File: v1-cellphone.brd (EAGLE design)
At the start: 91.4 x 44.5 mm, 55 parts, among them J1 AVRISP, J2 ZX62D-B-5P8, U1 MCP73831, U2 MEGA1284, U3 GSM_UC15, X1 BU-SMA-V, X2 CRYSTAL, X3 CCM03-3002 R102

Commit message: Ready for review at diy devices.
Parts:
- added C10: 18pF, rcl_custom:C0603
- added C17, C18: 100nF, cellphone-rcl:C1206
- added C19, C23: 100nF 16V, cellphone-rcl:C1206
- added C20, C24: 33pF 16V, cellphone-rcl:C1206
- added C21, C25: 10pF 16V, cellphone-rcl:C1206
- added C22, C26: 100uF 16V, cellphone-rcl:C1206
- added D1, D2, D3: (no value), SparkFun-DiscreteSemi:SMA-DIODE
- added D4: 5.1V, SparkFun-DiscreteSemi:SMB-DIODE
- added R11: 100, v1-cellphone:CELLPHONE-RCL_R1206
- added R12: 2K, v1-cellphone:CELLPHONE-RCL_R1206
- added TP1, TP2, TP3: TPPAD1-13, testpad:P1-13
- C12, C5: value 0.1uF -> 100nF
- C14: device cellphone-rcl:C1206 -> rcl_custom:C0603
- C15: value 18pF -> 100nF
- S1: device cellphone:B3U-1000P -> v1-cellphone:CELLPHONE_B3U-1000P
- X2: value CRYSTAL -> 16MHz
- moved C15 176.3 mm to (-54.6, -114.6), turned to 0 degrees
- moved C14 165.2 mm to (-55.6, -109.0), turned to 0 degrees
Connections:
- removed net SPK2P: U3.20
- removed net VCC: C11.+, C12.1, C13.1, C16.+, C4.1, J1.2, JP3.1, JP8.1, JP9.1, LED3.A, R4.2, U1.3, U2.17, U2.27, U2.38, U2.5
- removed net VDD_EXT: U3.7
- removed net VUSB: C3.1, J2.P1, LED1.A, U1.4
- new net 4.2V: C4.1, R11.2, U1.3
- new net 4V: C11.+, C12.1, C13.1, C15.1, C16.+, C17.1, C18.1, C19.1, C20.1, C21.1, C22.1, C23.1, C24.1, C25.1, C26.1, D4.C, JP3.1, JP8.1, JP9.1, LED3.A, R11.1, R12.2, R4.2, U2.17, U2.27, U2.38, U2.5, U3.50, U3.51, U3.52, U3.53
- new net 5V: C3.1, D1.C, D2.C, D3.C, LED1.A, U1.4
- new net N$10: D2.A, J1.2
- new net N$11: D3.A, JP7.4
- new net N$13: TP1.TP, U3.2
- new net N$14: TP2.TP, U3.7
- new net N$15: TP3.TP, U3.55
- new net N$9: D1.A, J2.P1
- net AGND: no longer U2.29
- net GND: now also C10.2, C17.2, C18.2, C19.2, C20.2, C21.2, C22.2, C23.2, C24.2, C25.2, C26.2, C5.1, D4.A, R12.1, U2.29; no longer C5.2
- net N$7: now also C10.1, X2.P$1; no longer C15.1, X2.P$2
- net N$8: now also X2.P$2; no longer X2.P$1
- net SHLD: now also C5.2; no longer C5.1
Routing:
- net VCC: track 111.3 -> 0.00 mm, vias 6 -> 0
- net 4V: track 0.00 -> 48.7 mm, vias 0 -> 5
- net VUSB: track 23.8 -> 0.00 mm
- net 5V: track 0.00 -> 23.8 mm
- net GND: track 38.9 -> 17.2 mm, vias 36 -> 35
- net N$8: track 8.00 -> 0.00 mm
- net N$7: track 7.92 -> 0.00 mm
- added copper zone on layer 1, net 4V
- added copper zone on layer 16, net 4V
- removed copper zone on layer 1, net VCC
- removed copper zone on layer 16, net VCC

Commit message: Added notes.
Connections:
- net RESET renamed !RESET
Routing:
- net !RESET: track 21.0 -> 18.3 mm
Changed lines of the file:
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@@
 <wire x1="34.036" y1="36.433" x2="-52.832" y2="-61.722" width="0" layer="19" extent="1-1"/>
 </signal>
-<signal name="RESET">
-<contactref element="R4" pad="1"/>
+<signal name="!RESET">
 <contactref element="C1" pad="2"/>
 <wire x1="47.879" y1="35.671" x2="47.879" y2="33.655" width="0.254" layer="1"/>
 <wire x1="47.879" y1="33.655" x2="47.879" y2="29.591" width="0.254" layer="1"/>
 <wire x1="47.879" y1="29.591" x2="50.188" y2="29.591" width="0.254" layer="1"/>
-<wire x1="38.109" y1="28.194" x2="37.855" y2="30.715" width="0.254" layer="16"/>
-<wire x1="37.855" y1="30.715" x2="37.954" y2="30.715" width="0.254" layer="16"/>
 <wire x1="47.879" y1="35.671" x2="39.732" y2="35.671" width="0.254" layer="1"/>
 <wire x1="46.088" y1="33.636" x2="47.86" y2="33.636" width="0.254" layer="1"/>
@@
 <contactref element="S1" pad="P$2"/>
 <contactref element="U2" pad="4"/>
+<contactref element="R4" pad="1"/>
 <wire x1="38.022" y1="28.194" x2="-50.292" y2="-64.262" width="0" layer="19" extent="16-16"/>
-<wire x1="38.109" y1="28.194" x2="38.022" y2="28.194" width="0" layer="19" extent="16-16"/>
-<wire x1="39.732" y1="35.671" x2="37.954" y2="30.715" width="0" layer="19" extent="1-16"/>
+<wire x1="37.855" y1="30.715" x2="38.022" y2="28.194" width="0" layer="19" extent="16-16"/>
+<wire x1="39.732" y1="35.671" x2="37.855" y2="30.715" width="0" layer="19" extent="1-16"/>
 <wire x1="50.188" y1="29.556" x2="50.188" y2="29.591" width="0" layer="19" extent="1-1"/>
 </signal>

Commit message: Version 1.2 with diode and power changes, package fixes to 0603.
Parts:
- removed D1, D2, D3: (no value), SparkFun-DiscreteSemi:SMA-DIODE
- removed D4: 5.1V, SparkFun-DiscreteSemi:SMB-DIODE
- removed JP1, JP5: (no value), pinhead:1X04
- removed JP2: (no value), v1-cellphone:PINHEAD_1X08
- removed JP4: (no value), pinhead:1X03
- removed JP6: (no value), v1-cellphone:PINHEAD_1X04
- removed JP8, JP9: BATTERY INPUT, SparkFun-Connectors:JST-2-SMD
- removed L23: 6.8nH Murata LQG18HN6N8J00D, SmartPrj:R0603-ROUND
- removed L24: 3.3nH Murata LQG18HN3N3S00D, SmartPrj:R0603-ROUND
- removed MIC1, MIC2, SPK: (no value), pinhead:1X02
- added C27, C28, C29, C33, C34, C35: 33pF 10V, rcl_custom:0603-B
- added C30, C31, C32, C36, C37, C38: 10pF 10V, rcl_custom:0603-B
- added J3: PA, SparkFun-Connectors:1X08_LOCK_LONGPADS
- added J4: PB, SparkFun-Connectors:1X04_LOCK_LONGPADS
- added J5: PC1, SparkFun-Connectors:1X03_LOCK_LONGPADS
- added J6: PC2, SparkFun-Connectors:1X04_LOCK_LONGPADS
- added J7: PD, SparkFun-Connectors:1X04_LOCK_LONGPADS
- added L1: 6.8nH Murata LQG18HN6N8J00D, rcl_custom:0603-B
- added L2: 3.3nH Murata LQG18HN3N3S00D, rcl_custom:0603-B
- added LED6: VCC, adafruit:CHIP-LED0603
- added Q1: MIC, adafruit:9.7ELECTRET
- added R13: 470, rcl_custom:0603-B
- added R14: 0 ohm, rcl_custom:0603-B
- added TP4, TP5, TP6, TP7, TP8, TP9: TPPAD1-13, testpad:P1-13
- C1: value 0.1 uF -> 100nF 16V; device cellphone-rcl:C1206 -> rcl_custom:0603-B
- C10, C14: device rcl_custom:C0603 -> rcl_custom:0603-B
- C12, C15, C17, C18, C5: value 100nF -> 100nF 16V; device cellphone-rcl:C1206 -> rcl_custom:0603-B
- C13: value 100nF 50V -> 100nF 16V; device cellphone-rcl:C1206 -> rcl_custom:0603-B
- C19, C20, C21, C22, C23, C24, C25, C26, C3, C4: device cellphone-rcl:C1206 -> rcl_custom:0603-B
- C2: value 100nF 50V -> 100nF 10V; device cellphone-rcl:C1206 -> rcl_custom:0603-B
- C6, C7, C9: value 33pF -> 33pF 10V; device cellphone-rcl:C1206 -> rcl_custom:0603-B
- C8: device SmartPrj:C0603-ROUND -> rcl_custom:0603-B
- J8: value (none) -> FTDI
- LED1: value (none) -> 5V; device v1-cellphone:CELLPHONE-LED_CHIP-LED0603 -> adafruit:CHIP-LED0603
- LED2: value (none) -> 3GSTAT; device cellphone-led:1206 -> adafruit:CHIP-LED0603
- LED3: value PWR -> VBAT; device cellphone-led:1206 -> adafruit:CHIP-LED0603
- LED4: value 13 -> DEBUG; device cellphone-led:1206 -> adafruit:CHIP-LED0603
- LED5: value (none) -> NETLIGHT; device cellphone-led:1206 -> adafruit:CHIP-LED0603
- R1, R10, R2, R3, R4, R5, R6, R9: device cellphone-rcl:R1206 -> rcl_custom:0603-B
- R11, R7, R8: device v1-cellphone:CELLPHONE-RCL_R1206 -> rcl_custom:0603-B
- R12: value 2K -> 2000; device v1-cellphone:CELLPHONE-RCL_R1206 -> rcl_custom:0603-B
- moved C1 256.3 mm to (-54.6, -202.7)
- moved R11 221.5 mm to (-54.6, -303.8)
- moved R12 221.5 mm to (-54.6, -309.9)
- renumbered JP3 to J9, JP7 to J8, SPEAKER to SP1
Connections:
- removed net 4.2V: C4.1, R11.2, U1.3
- removed net 4V: C11.+, C12.1, C13.1, C15.1, C16.+, C17.1, C18.1, C19.1, C20.1, C21.1, C22.1, C23.1, C24.1, C25.1, C26.1, D4.C, J9.1, JP8.1, JP9.1, LED3.A, R11.1, R12.2, R4.2, U2.17, U2.27, U2.38, U2.5, U3.50, U3.51, U3.52, U3.53
- removed net ANTENA: ANT1.FEED, C8.2, L24.2, X1.1
- removed net MIC1N: MIC2.2, U3.24
- removed net MIC1P: MIC2.1, U3.23
- removed net MIC2N: MIC1.2, U3.26
- removed net MIC2P: MIC1.1, U3.25
- removed net N$10: D2.A, J1.2
- removed net N$11: D3.A, J8.4
- new net ANTENNA: ANT1.FEED, C8.2, L2.2, X1.1
- new net N$16: C27.2, C28.1, C30.2, C31.1, Q1.+, U3.23
- new net N$19: C28.2, C29.1, C31.2, C32.1, Q1.-, U3.24
- new net STAT: R7.1, U1.1
- new net VBAT: C11.+, C13.1, C16.+, C4.1, J9.1, LED3.A, R11.2, U1.3
- new net VCC: C12.1, C15.1, C17.1, C18.1, C19.1, C20.1, C21.1, C22.1, C23.1, C24.1, C25.1, C26.1, LED6.A, R11.1, R12.2, R4.2, U2.17, U2.27, U2.38, U2.5, U3.50, U3.51, U3.52, U3.53
- net 5V: now also J1.2, J2.P1; no longer D1.C, D2.C, D3.C
- net AGND: now also C27.1, C29.2, C30.1, C32.2, C33.1, C35.2, C36.1, C38.2, L1.1, L2.1, R14.1; no longer L23.1, L24.1
- net ANT: now also L1.2; no longer L23.2
- net GND: now also R13.1, R14.2; no longer D4.A, JP8.2, JP9.2, R7.1, U1.1
- net N$9: now also LED6.C, R13.2; no longer D1.A, J2.P1
- net PA0: now also J3.1; no longer JP2.1
- net PA1: now also J3.2; no longer JP2.2
- net PA2: now also J3.3; no longer JP2.3
- net PA3: now also J3.4; no longer JP2.4
- net PA4: now also J3.5; no longer JP2.5
- net PA5: now also J3.6; no longer JP2.6
- net PA6: now also J3.7; no longer JP2.7
- net PA7: now also J3.8; no longer JP2.8
- net PB0: now also J4.1; no longer JP6.1
- net PB1: now also J4.2; no longer JP6.2
- net PB2: now also J4.3; no longer JP6.3
- net PB3: now also J4.4; no longer JP6.4
- net PC0: now also J5.1; no longer JP4.1
- net PC1: now also J5.2; no longer JP4.2
- net PC2: now also J5.3; no longer JP4.3
- net PC4: now also J6.1; no longer JP1.1
- net PC5: now also J6.2; no longer JP1.2
- net PC6: now also J6.3; no longer JP1.3
- net PC7: now also J6.4; no longer JP1.4
- net PD4: now also J7.1; no longer JP5.1
- net PD5: now also J7.2; no longer JP5.2
- net PD6: now also J7.3; no longer JP5.3
- net PD7: now also J7.4; no longer JP5.4
- net RXD1: now also TP5.TP
- net SIM_CLKR: now also TP8.TP
- net SIM_DATA: now also TP9.TP
- net SIM_RSTR: now also TP7.TP
- net SIM_VDD: now also TP6.TP
- net SPK1N: now also C34.2, C35.1, C37.2, C38.1; no longer SPK.1
- net SPK1P: now also C33.2, C34.1, C36.2, C37.1; no longer SPK.2
- net TXD1: now also TP4.TP
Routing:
- net PD5: track 61.5 -> 10.0 mm
- net VCC: track 0.00 -> 49.0 mm, vias 0 -> 5
- net 4V: track 48.7 -> 0.00 mm, vias 5 -> 0
- net SPK1N: track 24.2 -> 0.00 mm
- net SPK1P: track 20.6 -> 0.00 mm
- net !RESET: track 18.3 -> 0.00 mm
- net PC7: track 32.4 -> 16.2 mm
- net ANTENNA: track 0.00 -> 12.3 mm
- net ANTENA: track 12.1 -> 0.00 mm
- net PD4: track 19.5 -> 8.04 mm
- net PD6: track 20.9 -> 12.0 mm
- net PD7: track 21.6 -> 13.4 mm
- net PC1: track 24.4 -> 19.9 mm
- net PC2: track 27.4 -> 23.6 mm
- net PC4: track 25.8 -> 22.7 mm
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- added copper zone on layer 1, net VCC
- added copper zone on layer 16, net VCC
- removed copper zone on layer 1, net 4V
- removed copper zone on layer 16, net 4V

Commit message: Major power changes. Fixed 2.6V signal lines. Ready for review.
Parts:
- removed J6: PC2, SparkFun-Connectors:1X04_LOCK_LONGPADS
- removed J7: PD, SparkFun-Connectors:1X04_LOCK_LONGPADS
- removed LED6: VCC, adafruit:CHIP-LED0603
- added C39: 2.2uF, rcl_custom:0603-B
- added Q2, Q3: NTR4501N-D, max-viz:SOT-23
- added TP10, TP11, TP12, TP13, TP14, TP15, TP17: TPPAD1-13, testpad:P1-13
- added U4: TXB0104PWR, SparkFun-DigitalIC:TSSOP14
- C8: value 3.9pF Murata GQM1885C2A3R9BB01D -> 3.9pF 100V 0603
- J5: value PC1 -> PC; device SparkFun-Connectors:1X03_LOCK_LONGPADS -> SparkFun-Connectors:1X08_LOCK_LONGPADS
- L1: value 6.8nH Murata LQG18HN6N8J00D -> 6.8nH 430mA 0603
- L2: value 3.3nH Murata LQG18HN3N3S00D -> 3.3nH 500mA 0603
- R11: value 100 -> 4.99K
- R12: value 2000 -> 4.99K
- R13: value 470 -> 10K
- moved R11 195.3 mm to (-55.6, -499.1)
- moved R12 194.3 mm to (-55.6, -504.2)
- moved TP4 153.2 mm to (-55.4, -468.6)
- moved TP5 153.2 mm to (-55.4, -472.9)
- moved R13 122.9 mm to (-55.6, -509.3)
- moved J5 71.9 mm to (-55.4, -445.8)
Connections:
- removed net N$9: LED6.C, R13.2
- removed net PD4: J7.1, U2.13
- removed net PD5: J7.2, U2.14
- removed net PD6: J7.3, U2.15
- removed net PD7: J7.4, U2.16
- removed net PWRKEY: U2.22, U3.18
- removed net STAT: R7.1, U1.1
- removed net STATUS: LED2.A, U3.54
- removed net VCC: C12.1, C15.1, C17.1, C18.1, C19.1, C20.1, C21.1, C22.1, C23.1, C24.1, C25.1, C26.1, LED6.A, R11.1, R12.2, R4.2, U2.17, U2.27, U2.38, U2.5, U3.50, U3.51, U3.52, U3.53
- new net !PWRKEY: Q2.3, U3.18
- new net !UC15RESET: Q3.3, U3.17
- new net 2.6V: C39.1, R13.1, TP2.TP, U3.7, U4.1
- new net BATTSTATUS: R7.1, U1.1, U2.15
- new net N$10: TP10.TP, U3.11
- new net N$11: TP13.TP, X3.C6
- new net N$20: TP4.TP, U3.60, U4.2
- new net N$21: TP5.TP, U3.61, U4.3
- new net N$23: TP17.TP, U3.54, U4.5
- new net PC3: J5.4, U2.22
- new net SETPWRKEY: Q2.1, R11.2, TP12.TP, U2.13
- new net SETUC15RESET: Q3.1, R12.2, TP11.TP, U2.14
- new net UC15STATUS: LED2.A, U2.16, U4.10
- net 5V: now also J8.4
- net GND: now also C39.2, Q2.2, Q3.2, R11.1, U4.7; no longer R13.1
- net N$14: now also R13.2, U4.8; no longer TP2.TP, U3.7
- net PC4: now also J5.5; no longer J6.1
- net PC5: now also J5.6; no longer J6.2
- net PC6: now also J5.7; no longer J6.3
- net PC7: now also J5.8; no longer J6.4
- net RXD1: now also TP15.TP, U4.13; no longer TP5.TP, U3.60
- net TXD1: now also TP14.TP, U4.12; no longer TP4.TP, U3.61
- net VBAT: now also C12.1, C15.1, C17.1, C18.1, C19.1, C20.1, C21.1, C22.1, C23.1, C24.1, C25.1, C26.1, R4.2, U2.17, U2.27, U2.38, U2.5, U3.50, U3.51, U3.52, U3.53, U4.14; no longer R11.2
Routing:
- net VCC: track 49.0 -> 0.00 mm, vias 5 -> 0
- net VBAT: track 0.00 -> 49.0 mm, vias 0 -> 2
- net UC15STATUS: track 0.00 -> 19.4 mm
- net PWRKEY: track 19.3 -> 0.00 mm, vias 1 -> 0
- net BATTSTATUS: track 0.00 -> 13.8 mm
- net PD7: track 13.4 -> 0.00 mm
- net PD6: track 12.0 -> 0.00 mm
- net AGND: track 10.2 -> 0.00 mm
- net SETUC15RESET: track 0.00 -> 10.0 mm
- net PD5: track 10.0 -> 0.00 mm
- net SETPWRKEY: track 0.00 -> 8.04 mm
- net PD4: track 8.04 -> 0.00 mm
- net STATUS: track 6.03 -> 0.00 mm
- net STAT: track 1.82 -> 0.00 mm
- added copper zone on layer 1, net 3.8V
- added copper zone on layer 16, net 3.8V
- removed copper zone on layer 1, net VCC
- removed copper zone on layer 16, net VCC

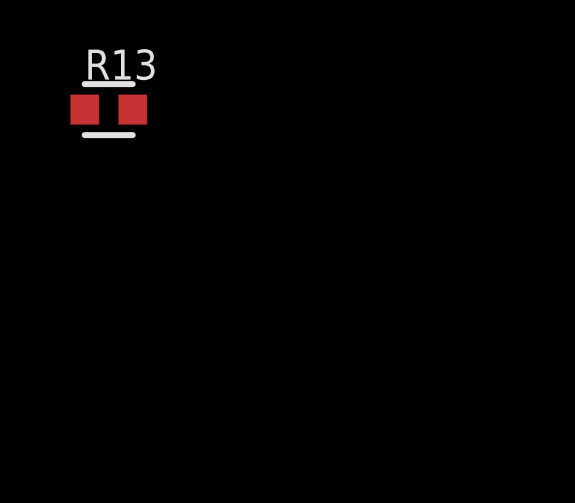
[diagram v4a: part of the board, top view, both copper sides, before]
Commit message: Added caps, made frames same size.
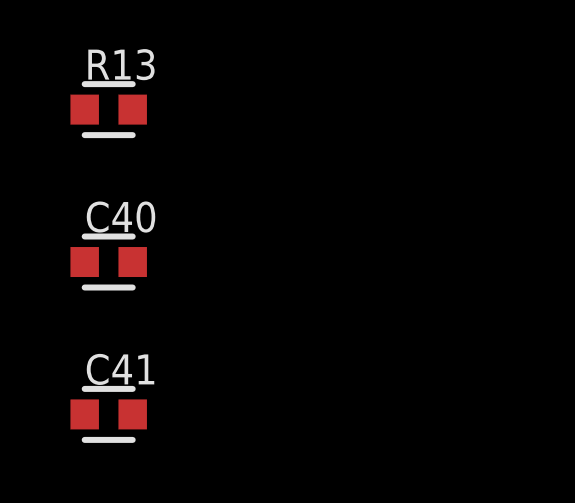
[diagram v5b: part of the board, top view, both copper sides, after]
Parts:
- added C40: 10nF 16V, rcl_custom:0603-B
- added C41: 100nF 16V, rcl_custom:0603-B
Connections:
- net !RESET: now also C40.1
- net GND: now also C40.2, C41.2
- net VBAT: now also C41.1
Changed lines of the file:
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@@
 <element name="R12" library="rcl_custom" package="0603-B" value="4.99K" x="-55.626" y="-504.19"/>
 <element name="R13" library="rcl_custom" package="0603-B" value="10K" x="-55.626" y="-509.27"/>
+<element name="C40" library="rcl_custom" package="0603-B" value="10nF 16V" x="-55.626" y="-514.35"/>
+<element name="C41" library="rcl_custom" package="0603-B" value="100nF 16V" x="-55.626" y="-519.43"/>
 </elements>
 <signals>
@@
 <via x="45.104" y="10.303" extent="1-16" drill="0.6096" shape="octagon"/>
 <via x="37.611" y="9.922" extent="1-16" drill="0.6096" shape="octagon"/>
-<contactref element="S1" pad="P$1"/>
 <contactref element="R10" pad="2"/>
 <polygon width="0.254" layer="16" isolate="0.254" thermals="no">
@@
 <contactref element="R12" pad="1"/>
 <contactref element="R11" pad="1"/>
+<contactref element="S1" pad="P$1"/>
+<contactref element="C40" pad="2"/>
+<contactref element="C41" pad="2"/>
 <wire x1="-53.81" y1="-169.418" x2="-53.81" y2="-175.514" width="0" layer="19" extent="1-1"/>
 <wire x1="-53.81" y1="-163.322" x2="-53.81" y2="-169.418" width="0" layer="19" extent="1-1"/>
@@
 <wire x1="-56.426" y1="-499.11" x2="-54.422" y2="-496.046" width="0" layer="19" extent="1-1"/>
 <wire x1="-56.426" y1="-504.19" x2="-56.426" y2="-499.11" width="0" layer="19" extent="1-1"/>
+<wire x1="-54.826" y1="-514.35" x2="-56.426" y2="-504.19" width="0" layer="19" extent="1-1"/>
+<wire x1="-54.826" y1="-519.43" x2="-54.826" y2="-514.35" width="0" layer="19" extent="1-1"/>
 </signal>
 <signal name="SIM_VDD">
@@
 <contactref element="J1" pad="5"/>
 <contactref element="C1" pad="2"/>
+<contactref element="R4" pad="1"/>
+<contactref element="C40" pad="1"/>
 <contactref element="S1" pad="P$2"/>
 <contactref element="U2" pad="4"/>
-<contactref element="R4" pad="1"/>
 <wire x1="38.022" y1="28.194" x2="-50.292" y2="-64.262" width="0" layer="19" extent="16-16"/>
 <wire x1="37.233" y1="30.715" x2="38.022" y2="28.194" width="0" layer="19" extent="16-16"/>
 <wire x1="50.188" y1="29.556" x2="38.022" y2="28.194" width="0" layer="19" extent="1-16"/>
 <wire x1="-53.81" y1="-202.692" x2="-50.292" y2="-64.262" width="0" layer="19" extent="1-1"/>
+<wire x1="-56.426" y1="-514.35" x2="-53.81" y2="-202.692" width="0" layer="19" extent="1-1"/>
 </signal>
 <signal name="N$5">
@@
 <wire x1="33.909" y1="35.306" x2="33.909" y2="37.468" width="0.254" layer="16"/>
 <contactref element="U4" pad="14"/>
+<contactref element="C41" pad="1"/>
 <wire x1="-55.41" y1="-169.418" x2="-55.41" y2="-175.514" width="0" layer="19" extent="1-1"/>
 <wire x1="-55.41" y1="-163.322" x2="-55.41" y2="-169.418" width="0" layer="19" extent="1-1"/>
@@
 <wire x1="87.11" y1="27.94" x2="61.788" y2="27.156" width="0" layer="19" extent="1-16"/>
 <wire x1="-54.782" y1="-483.7462" x2="-55.41" y2="-175.514" width="0" layer="19" extent="1-1"/>
+<wire x1="-56.426" y1="-519.43" x2="-54.782" y2="-483.7462" width="0" layer="19" extent="1-1"/>
 </signal>
 <signal name="BATTSTATUS" class="2">

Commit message: Verified packages. Minor tweaks throughout.
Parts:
- removed C16: 1mF 50V, cellphone-rcl:D/7343-31R
- removed J8: FTDI, cellphone:1X06-SMD-NOHOLES
- removed J9: BATTERY INPUT, SparkFun-Connectors:JST-2-SMD
- C11: device cellphone-rcl:D/7343-31R -> SparkFun-Capacitors:CPOL-RADIAL-1000UF-25V
- C2: value 100nF 10V -> 100nF 16V
- C27, C28, C29, C33, C35, C6, C7, C9: value 33pF 10V -> 33pF 16V
- C30: value 10pF 10V -> 10pF 10V
- C31, C32, C36, C37, C38: value 10pF 10V -> 10pF 16V
- C39: value 2.2uF -> 4.7uF 16V
- C4: value 4.7uF -> 4.7uF 16V
- J3: value PA -> GPIO; device SparkFun-Connectors:1X08_LOCK_LONGPADS -> SparkFun-Connectors:1X20_LOCK_LONGPADS
- J4: value PB -> FTDI; device SparkFun-Connectors:1X04_LOCK_LONGPADS -> SparkFun-Connectors:1X06_LOCK
- J5: value PC -> BATTERY INPUT; device SparkFun-Connectors:1X08_LOCK_LONGPADS -> SparkFun-Connectors:JST-2-SMD
- SP1: value SIREN -> SPEAKER
- X1: value BU-SMA-V -> SMA; device con-coax:BU-SMA-V -> v1-cellphone:CON-COAX_BU-SMA-V
- X2: value 16MHz -> 8MHz
- moved SP1 588.8 mm to (-54.4, -537.5), turned to 0 degrees
- moved Q2 513.0 mm to (78.2, 3.56)
- moved J5 488.3 mm to (5.33, 38.7), turned to 90 degrees
- moved C2 483.5 mm to (-55.6, -524.5)
- moved J4 398.8 mm to (89.2, 15.4), turned to 90 degrees
- moved J3 180.3 mm to (-55.4, -530.9)
- moved S1 55.8 mm to (88.4, 8.13)
- moved C11 16.3 mm to (19.4, 38.2)
- moved C3 1.83 mm to (15.7, 38.2)
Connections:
- net 5V: now also J4.4; no longer J8.4
- net GND: now also C11.2, J4.5, J4.6, J5.2; no longer C11.-, C16.-, J8.6, J9.2
- net N$5: now also J4.1; no longer J8.1
- net PB0: now also J3.9; no longer J4.1
- net PB1: now also J3.10; no longer J4.2
- net PB2: now also J3.11; no longer J4.3
- net PB3: now also J3.12; no longer J4.4
- net PC0: now also J3.13; no longer J5.1
- net PC1: now also J3.14; no longer J5.2
- net PC2: now also J3.15; no longer J5.3
- net PC3: now also J3.16; no longer J5.4
- net PC4: now also J3.17; no longer J5.5
- net PC5: now also J3.18; no longer J5.6
- net PC6: now also J3.19; no longer J5.7
- net PC7: now also J3.20; no longer J5.8
- net RXD0: now also J4.3; no longer J8.3
- net SPK1N: now also SP1.NEG; no longer SP1.P$1
- net SPK1P: now also SP1.POS; no longer SP1.P$2
- net TXD0: now also J4.2; no longer J8.2
- net VBAT: now also C11.1, J5.1; no longer C11.+, C16.+, J9.1
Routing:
- net SIM_VDD: track 83.3 -> 0.00 mm, vias 2 -> 0
- net N$5: track 59.2 -> 0.00 mm, vias 2 -> 0
- net SIM_CLKR: track 54.3 -> 0.00 mm, vias 2 -> 0
- net VBAT: track 49.0 -> 0.00 mm, vias 2 -> 0
- net SIM_RSTR: track 43.0 -> 0.00 mm, vias 2 -> 0
- net RXD0: track 42.8 -> 0.00 mm, vias 2 -> 0
- net TXD0: track 39.7 -> 0.00 mm, vias 2 -> 0
- net SIM_RST: track 36.1 -> 0.00 mm
- net SCK: track 34.0 -> 0.00 mm
- net MOSI: track 32.6 -> 0.00 mm, vias 2 -> 0
- net SIM_DATA: track 31.7 -> 0.00 mm, vias 2 -> 0
- net PC6: track 28.6 -> 0.00 mm
- net TXD1: track 27.4 -> 0.00 mm, vias 1 -> 0
- net PC5: track 26.1 -> 0.00 mm
- net RXD1: track 24.1 -> 0.00 mm, vias 1 -> 0
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- removed copper zone on layer 1, net 3.8V
- removed copper zone on layer 16, net 3.8V
- removed copper zone on layer 1, net GND
- removed copper zone on layer 16, net GND
- removed copper zone on layer 1, net VUSB
- removed copper zone on layer 16, net VUSB
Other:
- board size 91.4 x 44.5 mm -> 96 x 45.2 mm
- board text removed: "12"
- board text removed: "13"
- board text removed: "14"
- board text removed: "15"
- board text removed: "16"
- board text removed: "17"
- board text removed: "18"
- board text removed: "20"
- board text removed: "21"
- board text removed: "22"
- board text removed: "23"
- board text removed: "24"
- board text removed: "25"
- board text removed: "26"
- board text removed: "27"
- board text removed: "28"
- board text removed: "29"
- board text removed: "30"
- board text removed: "31"
- board text removed: "5"
- board text removed: "6"
- board text removed: "7"
- board text removed: "Cellphone Module David A. Mellis Nov. 26, 2013"
- board text removed: "GND"
- board text removed: "MIC"
- board text removed: "SPK"
- board text removed: "VCC"
